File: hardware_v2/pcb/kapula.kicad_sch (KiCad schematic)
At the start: 167 parts, among them J1 Conn_02x10_Odd_Even, J2 Conn_02x10_Odd_Even, J3 U.FL, J4 U.FL, J5 U.FL, J6 U.FL, Q1 AO3401A, Q1 BSS84, Q2 AO3400A, Q3 AO3400A, Q4 AO3400A, Q5 AO3401A, T1 BW21S7511A01TF, T2 BW21S7511A01TF, T3 BW21S7511A01TF, T4 BW21S7511A01TF, U1 TP4054, U2 DW01+G, U3 XC6206P332MR, U4 FM8002A, U5 EFR32FG14P233F256GM48-B, U6 TG2016SMN 38.4000M-MCGNNM3, U7 XA213-G4J, Y1 32768 Hz

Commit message: PCB: Change some resistor footprints and package sizes
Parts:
- R1, R13: footprint Resistor_SMD:R_0402_1005Metric -> Resistor_SMD:R_0603_1608Metric_Pad0.98x0.95mm_HandSolder; LCSC C17168 -> C21189
- R11, R12: footprint kapula:R_0402_to_0603_HandSolder -> Resistor_SMD:R_0402_1005Metric_Pad0.72x0.64mm_HandSolder
- R33, R34: footprint kapula:R_0402_to_0603_HandSolder -> Resistor_SMD:R_0603_1608Metric_Pad0.98x0.95mm_HandSolder
- R35, R48, R5: footprint kapula:R_0402_to_0603_HandSolder -> Resistor_SMD:R_0603_1608Metric_Pad0.98x0.95mm_HandSolder; LCSC C17168 -> C21189
- R44, R45, R46, R47: LCSC C17168 -> C21189
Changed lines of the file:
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@@
       (effects (font (size 1.27 1.27)))
     )
-    (property "Footprint" "kapula:R_0402_to_0603_HandSolder" (at 67.31 251.968 90)
+    (property "Footprint" "Resistor_SMD:R_0603_1608Metric_Pad0.98x0.95mm_HandSolder" (at 67.31 251.968 90)
       (effects (font (size 1.27 1.27)) hide)
     )
@@
       (effects (font (size 1.27 1.27)) (justify right))
     )
-    (property "Footprint" "kapula:R_0402_to_0603_HandSolder" (at 28.448 118.11 90)
+    (property "Footprint" "Resistor_SMD:R_0402_1005Metric_Pad0.72x0.64mm_HandSolder" (at 28.448 118.11 90)
       (effects (font (size 1.27 1.27)) hide)
     )
@@
       (effects (font (size 1.27 1.27)) (justify left))
     )
-    (property "Footprint" "kapula:R_0402_to_0603_HandSolder" (at 24.892 135.89 90)
+    (property "Footprint" "Resistor_SMD:R_0402_1005Metric_Pad0.72x0.64mm_HandSolder" (at 24.892 135.89 90)
       (effects (font (size 1.27 1.27)) hide)
     )
@@
       (effects (font (size 1.27 1.27)) hide)
     )
-    (property "LCSC" "C17168" (at 393.7 24.13 0)
+    (property "LCSC" "C21189" (at 393.7 24.13 0)
       (effects (font (size 1.27 1.27)) hide)
     )
@@
       (effects (font (size 1.27 1.27)) (justify right))
     )
-    (property "Footprint" "Resistor_SMD:R_0402_1005Metric" (at 50.038 40.64 90)
+    (property "Footprint" "Resistor_SMD:R_0603_1608Metric_Pad0.98x0.95mm_HandSolder" (at 50.038 40.64 90)
       (effects (font (size 1.27 1.27)) hide)
     )
@@
       (effects (font (size 1.27 1.27)) hide)
     )
-    (property "LCSC" "C17168" (at 48.26 40.64 0)
+    (property "LCSC" "C21189" (at 48.26 40.64 0)
       (effects (font (size 1.27 1.27)) hide)
     )
@@
       (effects (font (size 1.27 1.27)))
     )
-    (property "Footprint" "kapula:R_0402_to_0603_HandSolder" (at 96.52 240.538 90)
+    (property "Footprint" "Resistor_SMD:R_0603_1608Metric_Pad0.98x0.95mm_HandSolder" (at 96.52 240.538 90)
       (effects (font (size 1.27 1.27)) hide)
     )
@@
       (effects (font (size 1.27 1.27)))
     )
-    (property "Footprint" "kapula:R_0402_to_0603_HandSolder" (at 124.46 267.208 90)
+    (property "Footprint" "Resistor_SMD:R_0603_1608Metric_Pad0.98x0.95mm_HandSolder" (at 124.46 267.208 90)
       (effects (font (size 1.27 1.27)) hide)
     )
@@
       (effects (font (size 1.27 1.27)) hide)
     )
-    (property "LCSC" "C17168" (at 124.46 265.43 0)
+    (property "LCSC" "C21189" (at 124.46 265.43 0)
       (effects (font (size 1.27 1.27)) hide)
     )
@@
       (effects (font (size 1.27 1.27)))
     )
-    (property "Footprint" "kapula:R_0402_to_0603_HandSolder" (at 287.02 79.502 90)
+    (property "Footprint" "Resistor_SMD:R_0603_1608Metric_Pad0.98x0.95mm_HandSolder" (at 287.02 79.502 90)
       (effects (font (size 1.27 1.27)) hide)
     )
@@
       (effects (font (size 1.27 1.27)) hide)
     )
-    (property "LCSC" "C17168" (at 287.02 81.28 0)
+    (property "LCSC" "C21189" (at 287.02 81.28 0)
       (effects (font (size 1.27 1.27)) hide)
     )
@@
       (effects (font (size 1.27 1.27)) hide)
     )
-    (property "LCSC" "C17168" (at 393.7 31.75 0)
+    (property "LCSC" "C21189" (at 393.7 31.75 0)
       (effects (font (size 1.27 1.27)) hide)
     )
@@
       (effects (font (size 1.27 1.27)))
     )
-    (property "Footprint" "kapula:R_0402_to_0603_HandSolder" (at 195.58 28.448 90)
+    (property "Footprint" "Resistor_SMD:R_0603_1608Metric_Pad0.98x0.95mm_HandSolder" (at 195.58 28.448 90)
       (effects (font (size 1.27 1.27)) hide)
     )
@@
       (effects (font (size 1.27 1.27)) hide)
     )
-    (property "LCSC" "C17168" (at 195.58 26.67 0)
+    (property "LCSC" "C21189" (at 195.58 26.67 0)
       (effects (font (size 1.27 1.27)) hide)
     )
@@
       (effects (font (size 1.27 1.27)) hide)
     )
-    (property "LCSC" "C17168" (at 393.7 29.21 0)
+    (property "LCSC" "C21189" (at 393.7 29.21 0)
       (effects (font (size 1.27 1.27)) hide)
     )
@@
       (effects (font (size 1.27 1.27)))
     )
-    (property "Footprint" "Resistor_SMD:R_0402_1005Metric" (at 48.26 130.302 90)
+    (property "Footprint" "Resistor_SMD:R_0603_1608Metric_Pad0.98x0.95mm_HandSolder" (at 48.26 130.302 90)
       (effects (font (size 1.27 1.27)) hide)
     )
@@
       (effects (font (size 1.27 1.27)) hide)
     )
-    (property "LCSC" "C17168" (at 48.26 132.08 0)
+    (property "LCSC" "C21189" (at 48.26 132.08 0)
       (effects (font (size 1.27 1.27)) hide)
     )
@@
       (effects (font (size 1.27 1.27)) hide)
     )
-    (property "LCSC" "C17168" (at 393.7 26.67 0)
+    (property "LCSC" "C21189" (at 393.7 26.67 0)
       (effects (font (size 1.27 1.27)) hide)
     )

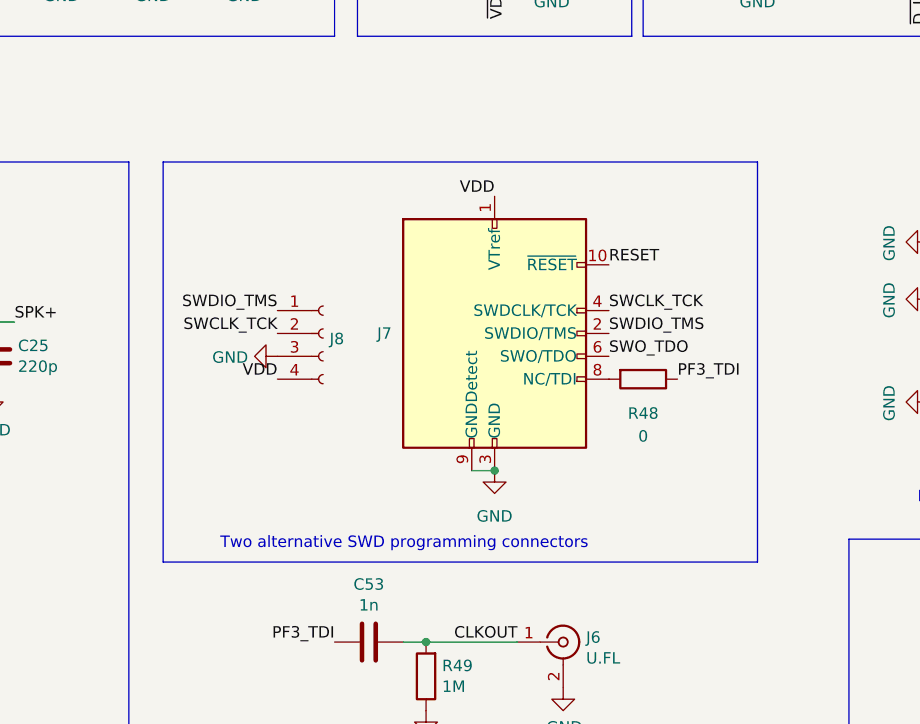
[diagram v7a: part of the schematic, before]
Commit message: PCB: Change SWD/JTAG connector to 2.54 mm pitch
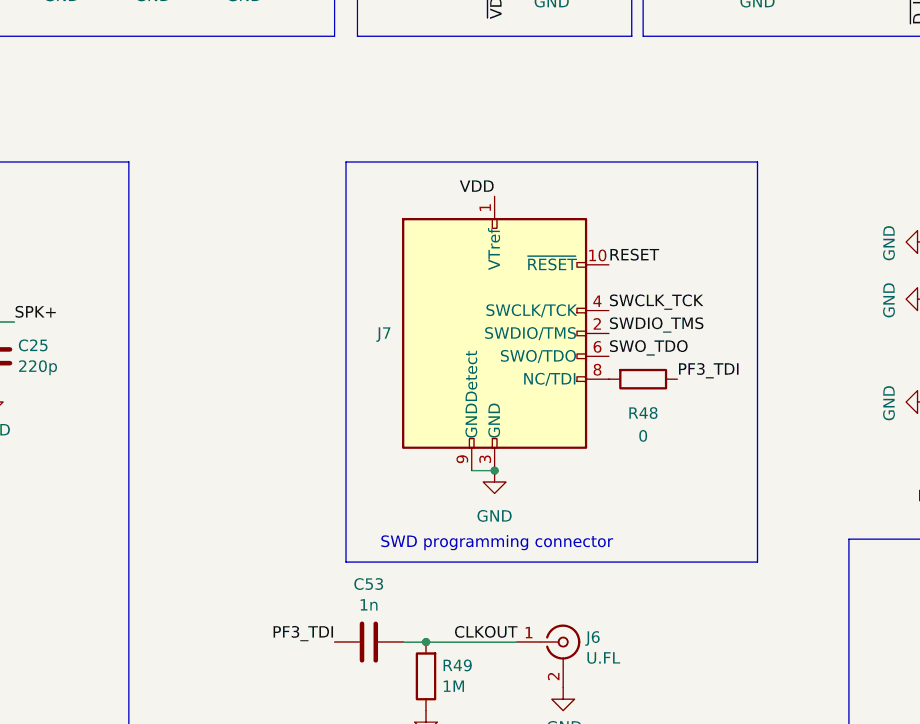
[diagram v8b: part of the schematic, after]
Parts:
- removed J8: ~, Connector_PinSocket_2.54mm:PinSocket_1x04_P2.54mm_Vertical, symbol Connector:Conn_01x04_Socket
- J7: footprint kapula:DZ127S-22-10-55 -> Connector_PinHeader_2.54mm:PinHeader_2x05_P2.54mm_Vertical; LCSC C5160761 -> (none)
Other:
- note added: "SWD programming connector"
- note removed: "Two alternative SWD programming connectors"
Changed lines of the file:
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@@
     (fill (type none))
   )
-  (rectangle (start 233.68 57.15) (end 299.72 101.6)
+  (rectangle (start 254 57.15) (end 299.72 101.6)
     (stroke (width 0) (type default))
     (fill (type none))
@@
     (effects (font (size 1.27 1.27)) (justify left bottom))
   )
-  (text "Two alternative SWD programming connectors" (at 240.03 100.33 0)
+  (text "SWD programming connector" (at 257.81 100.33 0)
     (effects (font (size 1.27 1.27)) (justify left bottom))
   )
@@
     (effects (font (size 1.27 1.27)) (justify left bottom))
   )
-  (label "SWDIO_TMS" (at 246.38 73.66 180) (fields_autoplaced)
-    (effects (font (size 1.27 1.27)) (justify right bottom))
-  )
   (label "VBAT" (at 26.67 114.3 180) (fields_autoplaced)
     (effects (font (size 1.27 1.27)) (justify right bottom))
@@
     (effects (font (size 1.27 1.27)) (justify right bottom))
   )
-  (label "SWCLK_TCK" (at 246.38 76.2 180) (fields_autoplaced)
-    (effects (font (size 1.27 1.27)) (justify right bottom))
-  )
   (label "PF3_TDI" (at 252.73 110.49 180) (fields_autoplaced)
     (effects (font (size 1.27 1.27)) (justify right bottom))
@@
     (effects (font (size 1.27 1.27)) (justify right bottom))
   )
-  (label "VDD" (at 246.38 81.28 180) (fields_autoplaced)
-    (effects (font (size 1.27 1.27)) (justify right bottom))
-  )
   (label "1V8" (at 92.71 238.76 180) (fields_autoplaced)
     (effects (font (size 1.27 1.27)) (justify right bottom))
@@
     )
   )
-  (symbol (lib_id "Connector:Conn_01x04_Socket") (at 251.46 76.2 0) (unit 1)
-    (in_bom yes) (on_board yes) (dnp no)
-    (property "Reference" "J8" (at 252.1712 76.8096 0)
-      (effects (font (size 1.27 1.27)) (justify left))
-    )
-    (property "Value" "~" (at 252.1712 79.121 0)
-      (effects (font (size 1.27 1.27)) (justify left))
-    )
-    (property "Footprint" "Connector_PinSocket_2.54mm:PinSocket_1x04_P2.54mm_Vertical" (at 251.46 76.2 0)
-      (effects (font (size 1.27 1.27)) hide)
-    )
-    (property "Datasheet" "" (at 251.46 76.2 0)
-      (effects (font (size 1.27 1.27)) hide)
-    )
-    (pin "1")
-    (pin "2")
-    (pin "3")
-    (pin "4")
-    (instances
-      (project "kapula"
-        (path "/f2315993-072e-45c9-8c85-e79c6d40aba4"
-          (reference "J8") (unit 1)
-        )
-      )
-    )
-  )
-  (symbol (lib_id "power:GND") (at 246.38 78.74 270) (unit 1)
-    (in_bom yes) (on_board yes) (dnp no)
-    (property "Reference" "#PWR0159" (at 240.03 78.74 0)
-      (effects (font (size 1.27 1.27)) hide)
-    )
-    (property "Value" "GND" (at 243.1288 78.867 90)
-      (effects (font (size 1.27 1.27)) (justify right))
-    )
-    (property "Footprint" "" (at 246.38 78.74 0)
-      (effects (font (size 1.27 1.27)) hide)
-    )
-    (property "Datasheet" "" (at 246.38 78.74 0)
-      (effects (font (size 1.27 1.27)) hide)
-    )
-    (pin "1")
-    (instances
-      (project "kapula"
-        (path "/f2315993-072e-45c9-8c85-e79c6d40aba4"
-          (reference "#PWR0159") (unit 1)
-        )
-      )
-    )
-  )
   (symbol (lib_id "Transistor_FET:AO3401A") (at 271.78 27.94 270) (mirror x) (unit 1)
     (in_bom yes) (on_board yes) (dnp no)
@@
       (effects (font (size 1.27 1.27)) (justify right))
     )
-    (property "Footprint" "kapula:DZ127S-22-10-55" (at 270.51 76.2 0)
-      (effects (font (size 1.27 1.27)) hide)
-    )
-    (property "Datasheet" "https://datasheet.lcsc.com/lcsc/2209141730_DEALON-DZ127S-22-10-55_C5160761.pdf" (at 261.62 107.95 90)
+    (property "Footprint" "Connector_PinHeader_2.54mm:PinHeader_2x05_P2.54mm_Vertical" (at 270.51 76.2 0)
       (effects (font (size 1.27 1.27)) hide)
     )
-    (property "LCSC" "C5160761" (at 270.51 76.2 0)
+    (property "Datasheet" "http://infocenter.arm.com/help/topic/com.arm.doc.ddi0314h/DDI0314H_coresight_components_trm.pdf" (at 261.62 107.95 90)
       (effects (font (size 1.27 1.27)) hide)
     )
